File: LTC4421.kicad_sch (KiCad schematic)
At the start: 59 parts, among them U2 LTC4421CG-PBF, U3 74LVC2G07GV,125, U4 74LVC2G07GV,125, U5 74LVC2G07GV,125

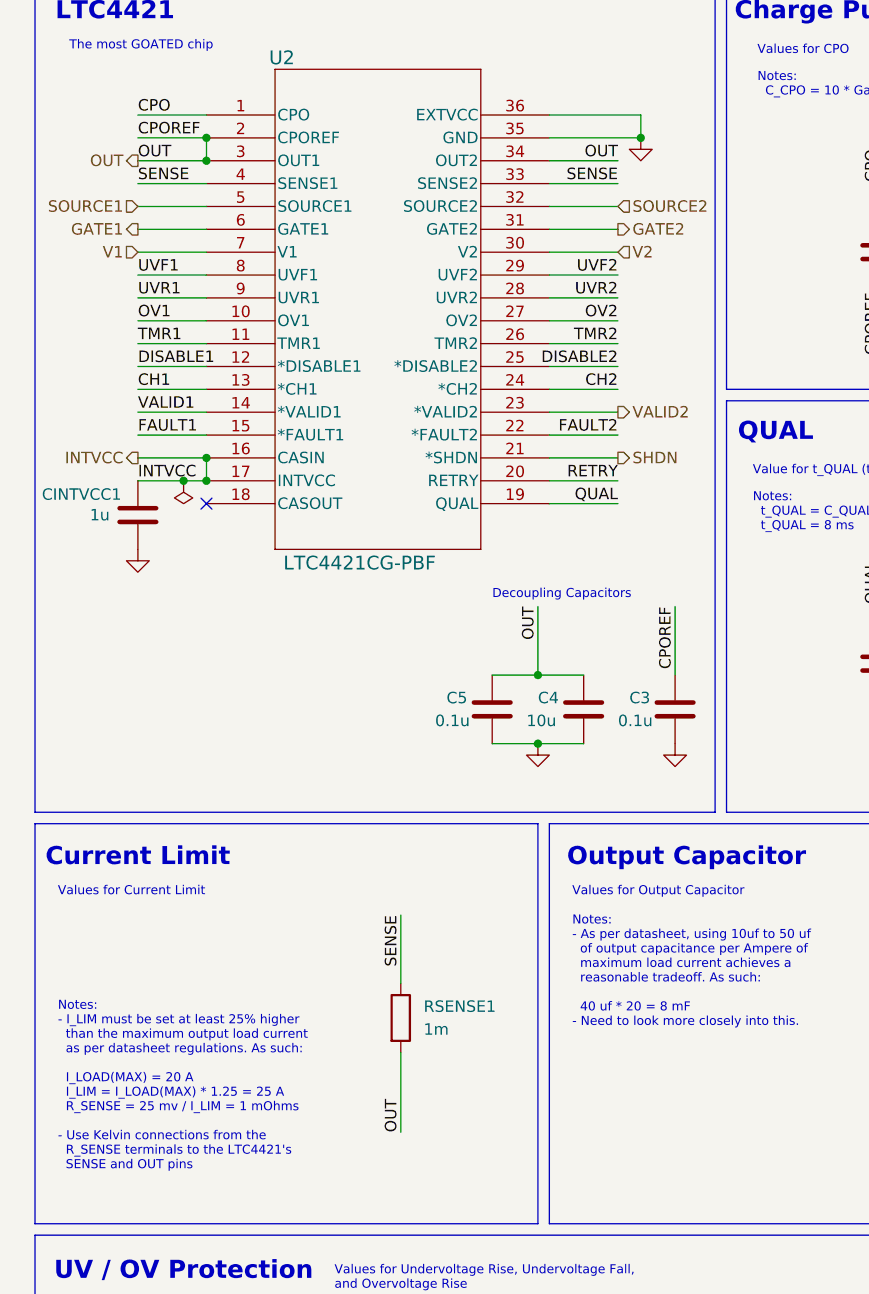
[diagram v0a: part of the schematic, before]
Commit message: added another current sense resistor
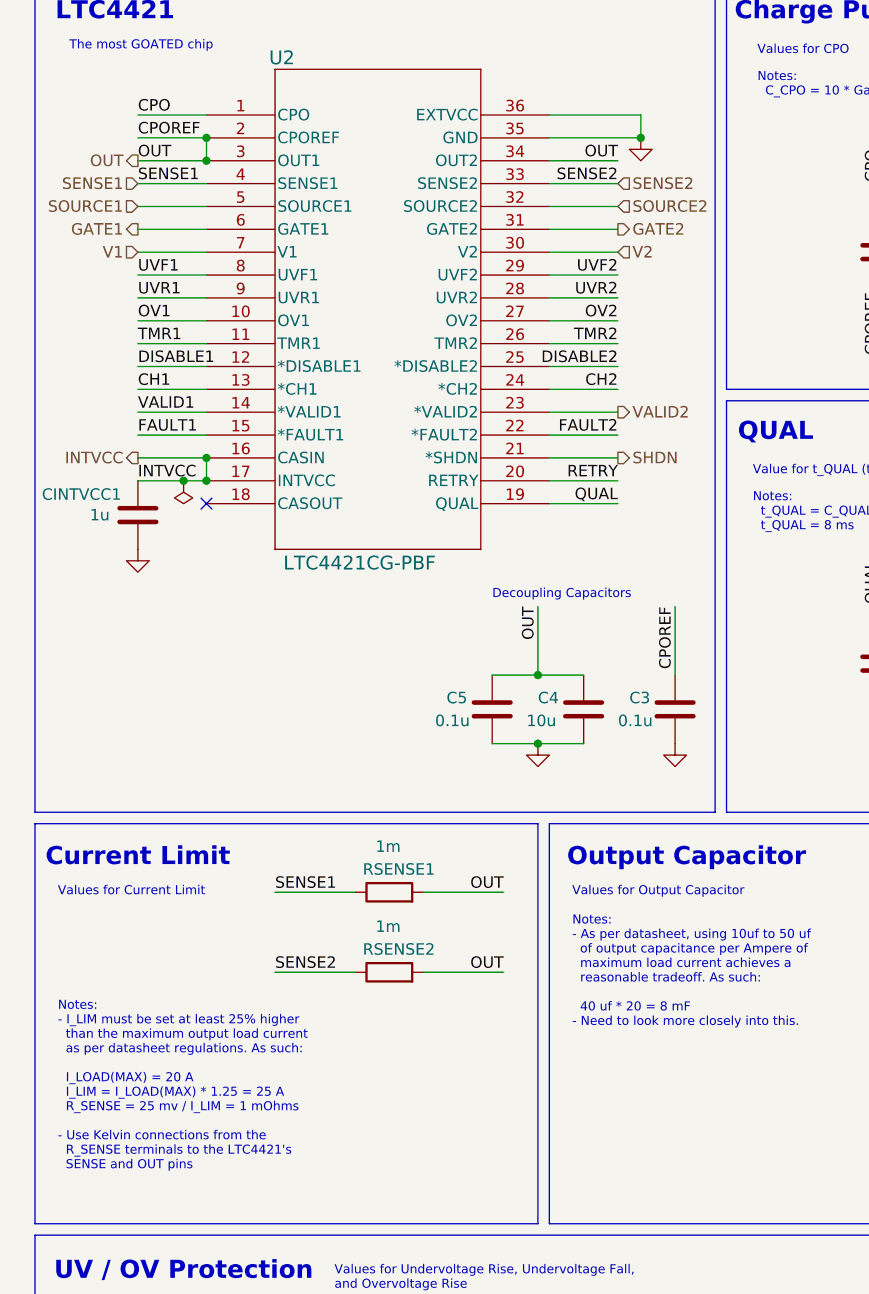
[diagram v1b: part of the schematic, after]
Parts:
- added RSENSE2: 1m, Resistor_SMD:R_0603_1608Metric, symbol Device:R
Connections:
- net OUT: now also RSENSE2.2
- net SENSE renamed SENSE1
- net SENSE1: no longer U2.33 (SENSE2)
- new net SENSE2: RSENSE2.1, U2.33 (SENSE2)
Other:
- moved on the sheet: RSENSE1
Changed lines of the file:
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@@
 	(wire
 		(pts
+			(xy 55.88 123.19) (xy 64.77 123.19)
+		)
+		(stroke
+			(width 0)
+			(type default)
+		)
+	)
+	(wire
+		(pts
 			(xy 160.02 182.88) (xy 160.02 187.96)
 		)
@@
 	(wire
 		(pts
+			(xy 39.37 114.3) (xy 48.26 114.3)
+		)
+		(stroke
+			(width 0)
+			(type default)
+		)
+	)
+	(wire
+		(pts
 			(xy 24.13 30.48) (xy 31.75 30.48)
 		)
@@
 	(wire
 		(pts
-			(xy 53.34 132.08) (xy 53.34 140.97)
+			(xy 55.88 114.3) (xy 64.77 114.3)
 		)
 		(stroke
@@
 	(wire
 		(pts
-			(xy 53.34 116.84) (xy 53.34 124.46)
+			(xy 251.46 99.06) (xy 251.46 85.09)
 		)
 		(stroke
@@
 	(wire
 		(pts
-			(xy 251.46 99.06) (xy 251.46 85.09)
+			(xy 133.35 44.45) (xy 139.7 44.45)
 		)
 		(stroke
@@
 	(wire
 		(pts
-			(xy 133.35 44.45) (xy 139.7 44.45)
+			(xy 24.13 45.72) (xy 31.75 45.72)
 		)
 		(stroke
@@
 	(wire
 		(pts
-			(xy 24.13 45.72) (xy 31.75 45.72)
+			(xy 106.68 77.47) (xy 106.68 85.09)
 		)
 		(stroke
@@
 	(wire
 		(pts
-			(xy 106.68 77.47) (xy 106.68 85.09)
+			(xy 130.81 68.58) (xy 139.7 68.58)
 		)
 		(stroke
@@
 	(wire
 		(pts
-			(xy 130.81 68.58) (xy 139.7 68.58)
+			(xy 207.01 148.59) (xy 207.01 160.02)
 		)
 		(stroke
@@
 	(wire
 		(pts
-			(xy 207.01 148.59) (xy 207.01 160.02)
+			(xy 39.37 123.19) (xy 48.26 123.19)
 		)
 		(stroke
@@
 		)
 	)
-	(label "SENSE"
+	(label "SENSE1"
 		(at 24.13 35.56 0)
 		(fields_autoplaced yes)
@@
 		)
 	)
-	(label "SENSE"
+	(label "SENSE2"
 		(at 77.47 35.56 180)
 		(fields_autoplaced yes)
@@
 		)
 	)
+	(label "OUT"
+		(at 64.77 123.19 180)
+		(fields_autoplaced yes)
+		(effects
+			(font
+				(size 1.27 1.27)
+			)
+			(justify right bottom)
+		)
+	)
 	(label "FAULT2"
 		(at 77.47 63.5 180)
@@
 		)
 	)
+	(label "SENSE2"
+		(at 39.37 123.19 0)
+		(fields_autoplaced yes)
+		(effects
+			(font
+				(size 1.27 1.27)
+			)
+			(justify left bottom)
+		)
+	)
 	(label "FAULT1"
 		(at 24.13 63.5 0)
@@
 	)
 	(label "OUT"
-		(at 53.34 140.97 90)
+		(at 64.77 114.3 180)
 		(fields_autoplaced yes)
 		(effects
@@
 				(size 1.27 1.27)
 			)
-			(justify left bottom)
+			(justify right bottom)
 		)
 	)
@@
 		)
 	)
-	(label "SENSE"
-		(at 53.34 116.84 270)
+	(label "SENSE1"
+		(at 39.37 114.3 0)
 		(fields_autoplaced yes)
 		(effects
@@
 				(size 1.27 1.27)
 			)
-			(justify right bottom)
+			(justify left bottom)
 		)
 	)
@@
 		)
 	)
+	(hierarchical_label "SENSE1"
+		(shape input)
+		(at 24.13 35.56 180)
+		(fields_autoplaced yes)
+		(effects
+			(font
+				(size 1.27 1.27)
+			)
+			(justify right)
+		)
+	)
 	(hierarchical_label "SHDN"
 		(shape output)
@@
 		)
 	)
+	(hierarchical_label "SENSE2"
+		(shape input)
+		(at 77.47 35.56 0)
+		(fields_autoplaced yes)
+		(effects
+			(font
+				(size 1.27 1.27)
+			)
+			(justify left)
+		)
+	)
 	(hierarchical_label "OUT"
 		(shape output)
@@
 	(symbol
 		(lib_id "Device:R")
+		(at 52.07 123.19 90)
+		(unit 1)
+		(exclude_from_sim no)
+		(in_bom yes)
+		(on_board yes)
+		(dnp no)
+		(property "Reference" "RSENSE2"
+			(at 57.15 120.65 90)
+			(effects
+				(font
+					(size 1.27 1.27)
+				)
+				(justify left)
+			)
+		)
+		(property "Value" "1m"
+			(at 53.34 118.11 90)
+			(effects
+				(font
+					(size 1.27 1.27)
+				)
+				(justify left)
+			)
+		)
+		(property "Footprint" "Resistor_SMD:R_0603_1608Metric"
+			(at 52.07 124.968 90)
+			(effects
+				(font
+					(size 1.27 1.27)
+				)
+				(hide yes)
+			)
+		)
+		(property "Datasheet" "https://mm.digikey.com/Volume0/opasdata/d220001/medias/docus/6352/YAGEO%20Datasheet_PA0603_1mR_L_0_RoHS_P_TCR.pdf"
+			(at 52.07 123.19 0)
+			(effects
+				(font
+					(size 1.27 1.27)
+				)
+				(hide yes)
+			)
+		)
+		(property "Description" "Resistor"
+			(at 52.07 123.19 0)
+			(effects
+				(font
+					(size 1.27 1.27)
+				)
+				(hide yes)
+			)
+		)
+		(property "Height" ""
+			(at 52.07 123.19 0)
+			(effects
+				(font
+					(size 1.27 1.27)
+				)
+				(hide yes)
+			)
+		)
+		(property "MFG PN" "PA0603FRP7W0R001L"
+			(at 52.07 123.19 0)
+			(effects
+				(font
+					(size 1.27 1.27)
+				)
+				(hide yes)
+			)
+		)
+		(property "P/N" ""
+			(at 52.07 123.19 0)
+			(effects
+				(font
+					(size 1.27 1.27)
+				)
+				(hide yes)
+			)
+		)
+		(property "Sim.Device" ""
+			(at 52.07 123.19 0)
+			(effects
+				(font
+					(size 1.27 1.27)
+				)
+				(hide yes)
+			)
+		)
+		(property "Sim.Pins" ""
+			(at 52.07 123.19 0)
+			(effects
+				(font
+					(size 1.27 1.27)
+				)
+				(hide yes)
+			)
+		)
+		(property "Sim.Type" ""
+			(at 52.07 123.19 0)
+			(effects
+				(font
+					(size 1.27 1.27)
+				)
+				(hide yes)
+			)
+		)
+		(pin "2"
+		)
+		(pin "1"
+		)
+		(instances
+			(project "Power-Secondary"
+				(path "/ba21eba1-72a9-489c-9498-a38516b9f252/3184e9c2-8c00-4ca3-a214-8a04df6b61e9"
+					(reference "RSENSE2")
+					(unit 1)
+				)
+			)
+		)
+	)
+	(symbol
+		(lib_id "Device:R")
 		(at 205.74 81.28 0)
 		(unit 1)
@@
 	(symbol
 		(lib_id "Device:R")
-		(at 53.34 128.27 0)
+		(at 52.07 114.3 90)
 		(unit 1)
 		(exclude_from_sim no)
@@
 		(on_board yes)
 		(dnp no)
-		(fields_autoplaced yes)
 		(property "Reference" "RSENSE1"
-			(at 55.88 126.9999 0)
+			(at 57.15 111.76 90)
 			(effects
 				(font
@@
 		)
 		(property "Value" "1m"
-			(at 55.88 129.5399 0)
+			(at 53.34 109.22 90)
 			(effects
 				(font
@@
 		)
 		(property "Footprint" "Resistor_SMD:R_0603_1608Metric"
-			(at 51.562 128.27 90)
+			(at 52.07 116.078 90)
 			(effects
 				(font
@@
 		)
 		(property "Datasheet" "https://mm.digikey.com/Volume0/opasdata/d220001/medias/docus/6352/YAGEO%20Datasheet_PA0603_1mR_L_0_RoHS_P_TCR.pdf"
-			(at 53.34 128.27 0)
+			(at 52.07 114.3 0)
 			(effects
 				(font
@@
 		)
 		(property "Description" "Resistor"
-			(at 53.34 128.27 0)
+			(at 52.07 114.3 0)
 			(effects
 				(font
@@
 		)
 		(property "Height" ""
-			(at 53.34 128.27 0)
+			(at 52.07 114.3 0)
 			(effects
 				(font
@@
 		)
 		(property "MFG PN" "PA0603FRP7W0R001L"
-			(at 53.34 128.27 0)
+			(at 52.07 114.3 0)
 			(effects
 				(font
@@
 		)
 		(property "P/N" ""
-			(at 53.34 128.27 0)
+			(at 52.07 114.3 0)
 			(effects
 				(font
@@
 		)
 		(property "Sim.Device" ""
-			(at 53.34 128.27 0)
+			(at 52.07 114.3 0)
 			(effects
 				(font
@@
 		)
 		(property "Sim.Pins" ""
-			(at 53.34 128.27 0)
+			(at 52.07 114.3 0)
 			(effects
 				(font
@@
 		)
 		(property "Sim.Type" ""
-			(at 53.34 128.27 0)
+			(at 52.07 114.3 0)
 			(effects
 				(font

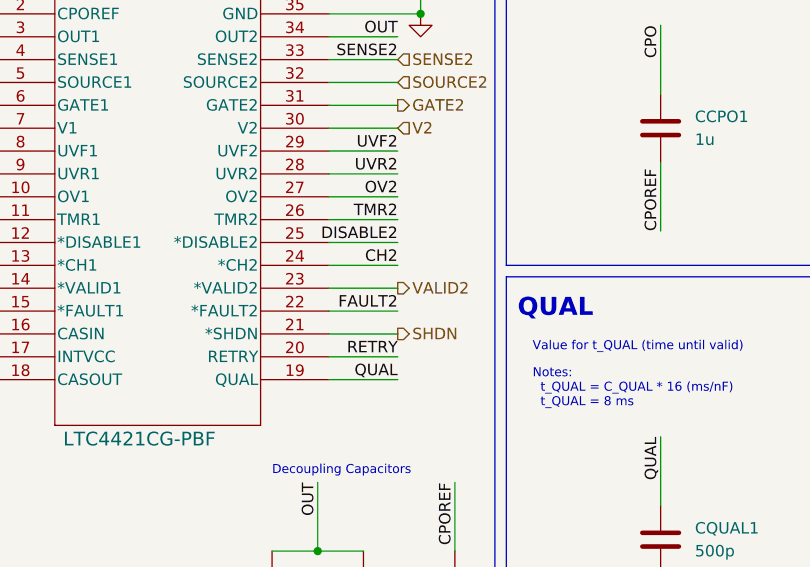
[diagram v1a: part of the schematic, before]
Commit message: change SHDN logic
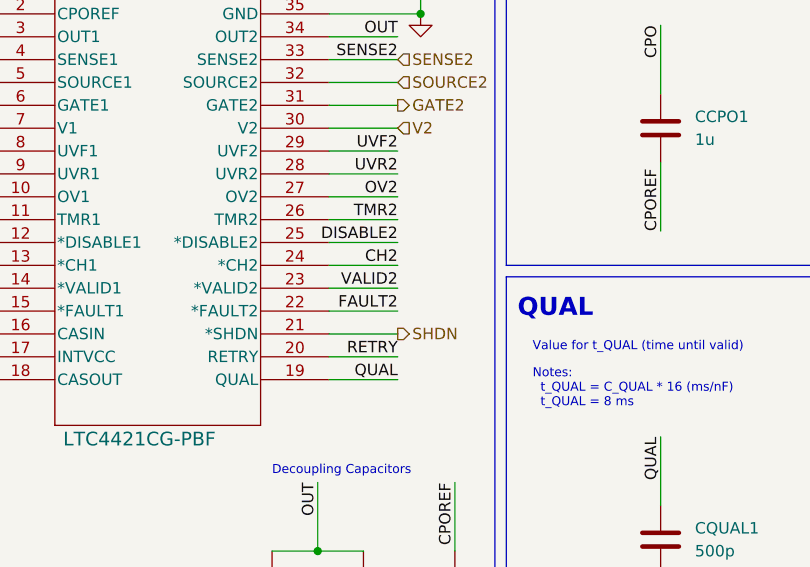
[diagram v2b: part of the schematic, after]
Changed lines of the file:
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@@
+		)
+	)
+	(label "VALID2"
+		(at 77.47 60.96 180)
+		(fields_autoplaced yes)
+		(effects
+			(font
+				(size 1.27 1.27)
+			)
+			(justify right bottom)
 		)
 	)
@@
 		(fields_autoplaced yes)
 		(effects
-			(font
-				(size 1.27 1.27)
-			)
-			(justify left)
-		)
-	)
-	(hierarchical_label "VALID2"
-		(shape output)
-		(at 77.47 60.96 0)
-		(fields_autoplaced yes)
-		(effects

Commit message: fixes to sch
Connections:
- net CH1: now also U5.1 (1A); no longer U5.3 (2A)
- net Non-Crit Drive: now also R16.2, U5.4 (2Y); no longer R14.2, U4.4 (2Y)
- net VALID1: now also U5.3 (2A); no longer U5.1 (1A)
- new net: R14.2, U4.4 (2Y)
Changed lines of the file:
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@@
 	)
 	(junction
-		(at 154.94 96.52)
-		(diameter 0)
-		(color 0 0 0 0)
-	)
-	(junction
 		(at 106.68 182.88)
 		(diameter 0)
@@
 	(wire
 		(pts
-			(xy 154.94 102.87) (xy 157.48 102.87)
-		)
-		(stroke
-			(width 0)
-			(type default)
-		)
-	)
-	(wire
-		(pts
 			(xy 158.75 36.83) (xy 158.75 38.1)
 		)
@@
 	(wire
 		(pts
-			(xy 154.94 96.52) (xy 154.94 102.87)
-		)
-		(stroke
-			(width 0)
-			(type default)
-		)
-	)
-	(wire
-		(pts
 			(xy 24.13 66.04) (xy 31.75 66.04)
 		)
@@
 	)
 	(label "VALID1"
-		(at 130.81 38.1 0)
+		(at 130.81 40.64 0)
 		(fields_autoplaced yes)
 		(effects
@@
 	)
 	(label "CH1"
-		(at 130.81 40.64 0)
+		(at 130.81 38.1 0)
 		(fields_autoplaced yes)
 		(effects
@@
 		)
 	)
+	(hierarchical_label "Non-Crit Drive"
+		(shape output)
+		(at 166.37 40.64 0)
+		(fields_autoplaced yes)
+		(effects
+			(font
+				(size 1.27 1.27)
+			)
+			(justify left)
+		)
+	)
 	(hierarchical_label "SHDN"
 		(shape output)
@@
 		)
 	)
-	(hierarchical_label "Non-Crit Drive"
-		(shape output)
-		(at 157.48 102.87 0)
-		(fields_autoplaced yes)
-		(effects
-			(font
-				(size 1.27 1.27)
-			)
-			(justify left)
-		)
-	)

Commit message: layout complete
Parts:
- removed TP2: TestPoint, UTSVT_Special:TestPoint_HEX_3mmID, symbol Connector:TestPoint
- RSENSE1, RSENSE2: footprint Resistor_SMD:R_0603_1608Metric -> PowerBoardLib:RESC6432X89N
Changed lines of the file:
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@@
 	(wire
 		(pts
-			(xy 194.31 148.59) (xy 194.31 160.02)
-		)
-		(stroke
-			(width 0)
-			(type default)
-		)
-	)
-	(wire
-		(pts
 			(xy 205.74 73.66) (xy 205.74 77.47)
 		)
@@
 		)
 	)
-	(label "CPO"
-		(at 194.31 160.02 90)
-		(fields_autoplaced yes)
-		(effects
-			(font
-				(size 1.27 1.27)
-			)
-			(justify left bottom)
-		)
-	)
 	(label "TMR2"
 		(at 160.02 167.64 270)
@@
 	)
 	(symbol
-		(lib_id "Connector:TestPoint")
-		(at 194.31 148.59 0)
-		(unit 1)
-		(exclude_from_sim no)
-		(in_bom yes)
-		(on_board yes)
-		(dnp no)
-		(fields_autoplaced yes)
-		(property "Reference" "TP2"
-			(at 196.85 144.0179 0)
-			(effects
-				(font
-					(size 1.27 1.27)
-				)
-				(justify left)
-			)
-		)
-		(property "Value" "TestPoint"
-			(at 196.85 146.5579 0)
-			(effects
-				(font
-					(size 1.27 1.27)
-				)
-				(justify left)
-			)
-		)
-		(property "Footprint" "UTSVT_Special:TestPoint_HEX_3mmID"
-			(at 199.39 148.59 0)
-			(effects
-				(font
-					(size 1.27 1.27)
-				)
-				(hide yes)
-			)
-		)
-		(property "Datasheet" "~"
-			(at 199.39 148.59 0)
-			(effects
-				(font
-					(size 1.27 1.27)
-				)
-				(hide yes)
-			)
-		)
-		(property "Description" "test point"
-			(at 194.31 148.59 0)
-			(effects
-				(font
-					(size 1.27 1.27)
-				)
-				(hide yes)
-			)
-		)
-		(property "Height" ""
-			(at 194.31 148.59 0)
-			(effects
-				(font
-					(size 1.27 1.27)
-				)
-				(hide yes)
-			)
-		)
-		(property "MFG PN" ""
-			(at 194.31 148.59 0)
-			(effects
-				(font
-					(size 1.27 1.27)
-				)
-				(hide yes)
-			)
-		)
-		(property "P/N" ""
-			(at 194.31 148.59 0)
-			(effects
-				(font
-					(size 1.27 1.27)
-				)
-				(hide yes)
-			)
-		)
-		(property "Sim.Device" ""
-			(at 194.31 148.59 0)
-			(effects
-				(font
-					(size 1.27 1.27)
-				)
-				(hide yes)
-			)
-		)
-		(property "Sim.Pins" ""
-			(at 194.31 148.59 0)
-			(effects
-				(font
-					(size 1.27 1.27)
-				)
-				(hide yes)
-			)
-		)
-		(property "Sim.Type" ""
-			(at 194.31 148.59 0)
-			(effects
-				(font
-					(size 1.27 1.27)
-				)
-				(hide yes)
-			)
-		)
-		(pin "1"
-		)
-		(instances
-			(project "Power-Secondary"
-				(path "/ba21eba1-72a9-489c-9498-a38516b9f252/3184e9c2-8c00-4ca3-a214-8a04df6b61e9"
-					(reference "TP2")
-					(unit 1)
-				)
-			)
-		)
-	)
-	(symbol
 		(lib_id "Device:R")
 		(at 158.75 88.9 0)
@@
 			)
 		)
-		(property "Footprint" "Resistor_SMD:R_0603_1608Metric"
+		(property "Footprint" "PowerBoardLib:RESC6432X89N"
 			(at 52.07 124.968 90)
 			(effects
@@
 			)
 		)
-		(property "Footprint" "Resistor_SMD:R_0603_1608Metric"
+		(property "Footprint" "PowerBoardLib:RESC6432X89N"
 			(at 52.07 116.078 90)
 			(effects

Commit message: Layout fixes
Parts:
- JP1, JP2, JP3: footprint Connector_PinHeader_1.00mm:PinHeader_1x03_P1.00mm_Vertical -> Connector_PinHeader_2.54mm:PinHeader_1x03_P2.54mm_Vertical
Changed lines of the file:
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@@
 			)
 		)
-		(property "Footprint" "Connector_PinHeader_1.00mm:PinHeader_1x03_P1.00mm_Vertical"
+		(property "Footprint" "Connector_PinHeader_2.54mm:PinHeader_1x03_P2.54mm_Vertical"
 			(at 194.31 121.92 0)
 			(effects
@@
 			)
 		)
-		(property "Footprint" "Connector_PinHeader_1.00mm:PinHeader_1x03_P1.00mm_Vertical"
+		(property "Footprint" "Connector_PinHeader_2.54mm:PinHeader_1x03_P2.54mm_Vertical"
 			(at 261.62 121.92 0)
 			(effects
@@
 			)
 		)
-		(property "Footprint" "Connector_PinHeader_1.00mm:PinHeader_1x03_P1.00mm_Vertical"
+		(property "Footprint" "Connector_PinHeader_2.54mm:PinHeader_1x03_P2.54mm_Vertical"
 			(at 228.6 121.92 0)
 			(effects

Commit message: made all planes solid filled
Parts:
- JP1, JP2, JP3: footprint Connector_PinHeader_2.54mm:PinHeader_1x03_P2.54mm_Vertical -> Connector_PinHeader_1.00mm:PinHeader_1x03_P1.00mm_Vertical
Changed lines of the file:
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@@
 			)
 		)
-		(property "Footprint" "Connector_PinHeader_2.54mm:PinHeader_1x03_P2.54mm_Vertical"
+		(property "Footprint" "Connector_PinHeader_1.00mm:PinHeader_1x03_P1.00mm_Vertical"
 			(at 194.31 121.92 0)
 			(effects
@@
 			)
 		)
-		(property "Footprint" "Connector_PinHeader_2.54mm:PinHeader_1x03_P2.54mm_Vertical"
+		(property "Footprint" "Connector_PinHeader_1.00mm:PinHeader_1x03_P1.00mm_Vertical"
 			(at 261.62 121.92 0)
 			(effects
@@
 			)
 		)
-		(property "Footprint" "Connector_PinHeader_2.54mm:PinHeader_1x03_P2.54mm_Vertical"
+		(property "Footprint" "Connector_PinHeader_1.00mm:PinHeader_1x03_P1.00mm_Vertical"
 			(at 228.6 121.92 0)
 			(effects

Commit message: gerbers
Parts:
- R30, R8: value 215K -> 226K
- R31, R5: value 5.76M -> 5.69M
- R32, R6: value 287K -> 277K
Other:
- note added: "OV1 = 13.2 V UVR1 = 11.5 V UVF1 = 10.8 V"
- note added: "Reference excel calculations:"
- note removed: "OV1 = 13 V UVR1 = 11.5 V UVF1 = 10.5 V"
- note removed: "Reference excel calculations: R6 = R4 = R2 = 5760 kOhms R1 = 287 kOhms R3 = 261 kOhms R5 = 215 kOhms"
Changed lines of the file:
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@@
 		)
 	)
-	(text "OV1 = 13 V\nUVR1 = 11.5 V\nUVF1 = 10.5 V"
+	(text "OV1 = 13.2 V\nUVR1 = 11.5 V\nUVF1 = 10.8 V"
 		(exclude_from_sim no)
 		(at 111.252 157.226 0)
@@
 		)
 	)
-	(text "Reference excel calculations:\nR6 = R4 = R2 = 5760 kOhms\nR1 = 287 kOhms\nR3 = 261 kOhms\nR5 = 215 kOhms"
+	(text "Reference excel calculations:\n\n"
 		(exclude_from_sim no)
 		(at 39.624 164.592 0)
@@
 			)
 		)
-		(property "Value" "5.76M"
+		(property "Value" "5.69M"
 			(at 109.22 180.3399 0)
 			(effects
@@
 			)
 		)
-		(property "Value" "287K"
+		(property "Value" "277K"
 			(at 57.15 187.9599 0)
 			(effects
@@
 			)
 		)
-		(property "Value" "287K"
+		(property "Value" "277K"
 			(at 109.22 187.9599 0)
 			(effects
@@
 			)
 		)
-		(property "Value" "5.76M"
+		(property "Value" "5.69M"
 			(at 57.15 180.3399 0)
 			(effects
@@
 			)
 		)
-		(property "Value" "215K"
+		(property "Value" "226K"
 			(at 76.2 187.9599 0)
 			(effects
@@
 			)
 		)
-		(property "Value" "215K"
+		(property "Value" "226K"
 			(at 24.13 187.9599 0)
 			(effects
